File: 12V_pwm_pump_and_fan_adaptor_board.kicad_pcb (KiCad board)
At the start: 2 copper layers, 190 x 40 mm, 3 parts, among them J1 39-30-0080

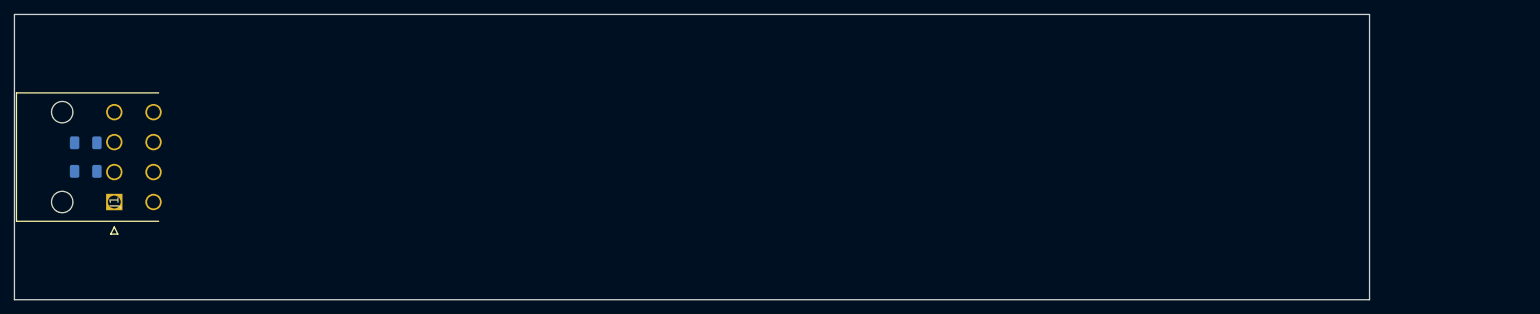
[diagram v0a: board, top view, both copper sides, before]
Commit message: feat: add connector footprint and update PCB layout and schematic files
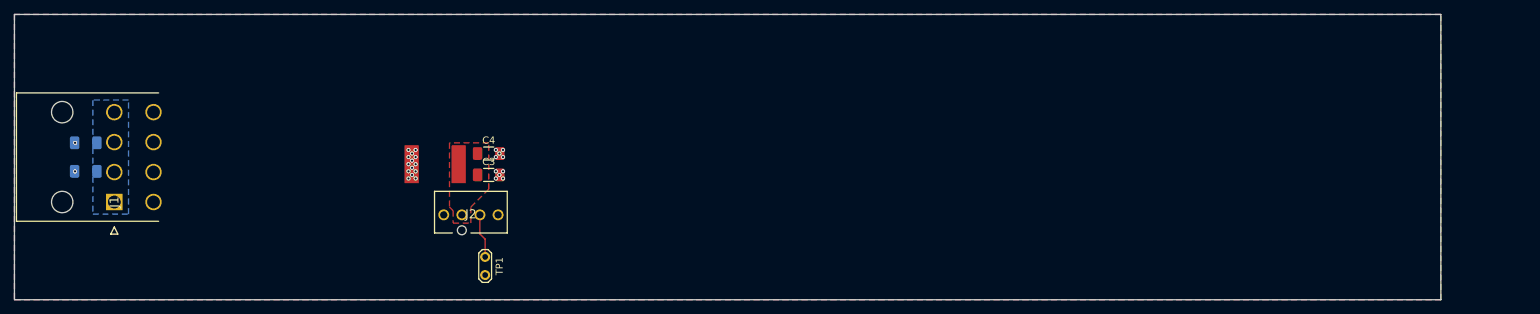
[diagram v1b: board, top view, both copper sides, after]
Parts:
- added C3: C, Capacitor_SMD:C_1206_3216Metric_Pad1.33x1.80mm_HandSolder, F.Cu at (86.5, 42.5)
- added C4: C, Capacitor_SMD:C_1206_3216Metric_Pad1.33x1.80mm_HandSolder, F.Cu at (86.5, 39.5)
- added FUSE1: ~, fuses:SMD2920P500TF16, F.Cu at (79.0, 41.0)
- added J2: Fan_4pin, connectors:0470531000, F.Cu at (80.2, 48.1)
- added TP1: TestPoint_2Pole, TestPoint:TestPoint_2Pads_Pitch2.54mm_Drill0.8mm, F.Cu at (86.0, 54.0)
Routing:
- net Net-(J2-TACH): track 0.00 -> 6.20 mm
- net GND: vias 0 -> 12
- net +12V: vias 0 -> 14
- added copper zone on B.Cu, net +12V
- added copper zone on In2.Cu, net +12V
- added copper zone on B.Cu, net GND
- added copper zone on F.Cu, net GND
- added copper zone on In1.Cu, net GND
- added copper zone on F.Cu, net Net-(J2-+12V)
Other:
- board size 190 x 40 mm -> 200 x 40 mm
- copper layers 2 -> 4

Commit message: feat: add 3D model for 350424-1 connector to library
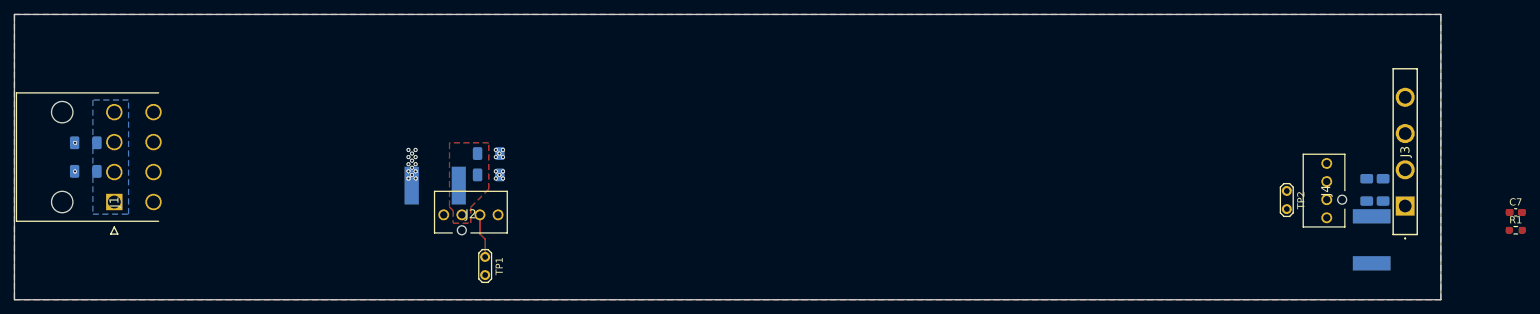
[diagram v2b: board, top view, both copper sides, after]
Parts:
- added C5: C, Capacitor_SMD:C_1206_3216Metric_Pad1.33x1.80mm_HandSolder, B.Cu at (209.6, 44.6)
- added C6: C, Capacitor_SMD:C_1206_3216Metric_Pad1.33x1.80mm_HandSolder, B.Cu at (211.9, 44.6)
- added C7: C, Capacitor_SMD:C_0603_1608Metric_Pad1.08x0.95mm_HandSolder, F.Cu at (230.5, 47.8)
- added FUSE2: ~, fuses:SMD2920P500TF16, B.Cu at (210.3, 51.6)
- added J3: 350424-1, connectors:350424-1, F.Cu at (215.0, 46.9)
- added J4: Fan_4pin, connectors:0470531000, F.Cu at (204.0, 48.5)
- added R1: R, Resistor_SMD:R_0603_1608Metric_Pad0.98x0.95mm_HandSolder, F.Cu at (230.5, 50.3)
- added TP2: TestPoint_2Pole, TestPoint:TestPoint_2Pads_Pitch2.54mm_Drill0.8mm, F.Cu at (198.4, 44.8)
- C3, C4, FUSE1: moved to B.Cu
- moved FUSE1 3.00 mm to (79.0, 44.0), turned to -90 degrees

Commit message: chore: update KiCad project settings and sync internal revision history
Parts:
- added C10: C, Capacitor_SMD:C_1206_3216Metric_Pad1.33x1.80mm_HandSolder, B.Cu at (116.1, 37.4)
- added C11: C, Capacitor_SMD:C_0603_1608Metric_Pad1.08x0.95mm_HandSolder, F.Cu at (115.9, 44.9)
- added C12: C, Capacitor_SMD:C_1206_3216Metric_Pad1.33x1.80mm_HandSolder, B.Cu at (138.9, 37.4)
- added C13: C, Capacitor_SMD:C_1206_3216Metric_Pad1.33x1.80mm_HandSolder, B.Cu at (146.1, 37.4)
- added C14: C, Capacitor_SMD:C_0603_1608Metric_Pad1.08x0.95mm_HandSolder, F.Cu at (145.9, 44.9)
- added C8: C, Capacitor_SMD:C_0603_1608Metric_Pad1.08x0.95mm_HandSolder, F.Cu at (85.9, 44.9)
- added C9: C, Capacitor_SMD:C_1206_3216Metric_Pad1.33x1.80mm_HandSolder, B.Cu at (108.9, 37.4)
- added FUSE3: ~, fuses:SMD2920P500TF16, B.Cu at (112.5, 31.8)
- added FUSE4: ~, fuses:SMD2920P500TF16, B.Cu at (142.5, 31.8)
- added J5: Fan_4pin, connectors:0470531000, F.Cu at (31.0, 55.2)
- added J6: Fan_4pin, connectors:0470531000, F.Cu at (110.0, 40.0)
- added J7: Fan_4pin, connectors:0470531000, F.Cu at (140.0, 40.0)
- added R2: R, Resistor_SMD:R_0603_1608Metric_Pad0.98x0.95mm_HandSolder, F.Cu at (86.7, 47.3)
- added R3: R, Resistor_SMD:R_0603_1608Metric_Pad0.98x0.95mm_HandSolder, F.Cu at (116.7, 47.3)
- added R4: R, Resistor_SMD:R_0603_1608Metric_Pad0.98x0.95mm_HandSolder, F.Cu at (146.7, 47.3)
- added TP3: TestPoint_2Pole, TestPoint:TestPoint_2Pads_Pitch2.54mm_Drill0.8mm, F.Cu at (112.4, 45.6)
- added TP4: TestPoint_2Pole, TestPoint:TestPoint_2Pads_Pitch2.54mm_Drill0.8mm, F.Cu at (142.4, 45.6)
- moved R1 33.9 mm to (196.7, 52.2)
- moved C7 31.5 mm to (199.2, 51.4), turned to 90 degrees
- moved FUSE1 12.7 mm to (82.5, 31.8), turned to 180 degrees
- moved TP1 9.16 mm to (82.4, 45.6), turned to 180 degrees
- moved J2 8.10 mm to (80.0, 40.0)
- moved C4 7.88 mm to (78.9, 37.4), turned to 180 degrees
- moved C3 5.12 mm to (86.1, 37.4)
- moved TP2 3.41 mm to (198.7, 48.1), turned to 90 degrees
- moved J4 2.82 mm to (204.1, 45.7), turned to -90 degrees
- moved C6 2.80 mm to (209.1, 44.7), turned to 90 degrees
- moved C5 2.10 mm to (211.7, 44.7), turned to 90 degrees
- moved FUSE2 0.22 mm to (210.4, 51.8), turned to 0 degrees
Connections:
- J2 pad 4: /output_connectors/12V_pwm_fan_output_connector/shared_pwm_signal -> Net-(J2-PWM)
- R1 pad 1: /output_connectors/12V_pwm_pump_connector/shared_pwm_signal -> /output_connectors/shared_pwm_signal
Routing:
- net /output_connectors/shared_pwm_signal: track 0.00 -> 161.7 mm
- net Net-(J4-PWM): track 0.00 -> 6.95 mm
- net Net-(J7-PWM): track 0.00 -> 6.77 mm
- net Net-(J6-PWM): track 0.00 -> 6.77 mm
- net Net-(J2-PWM): track 0.00 -> 6.77 mm
- net Net-(J7-TACH): track 0.00 -> 6.73 mm
- net Net-(J6-TACH): track 0.00 -> 6.73 mm
- net Net-(J4-TACH): track 0.00 -> 6.48 mm
- net Net-(J2-TACH): track 6.20 -> 6.73 mm
- net GND: vias 12 -> 43
- net +12V: vias 14 -> 0
- added copper zone on In2.Cu, net GND
- added copper zone on B.Cu, net Net-(J2-+12V)
- added copper zone on B.Cu, net Net-(J3-+12V)
- added copper zone on B.Cu, net Net-(J6-+12V)
- added copper zone on B.Cu, net Net-(J7-+12V)
- removed copper zone on In2.Cu, net +12V
- removed copper zone on F.Cu, net Net-(J2-+12V)

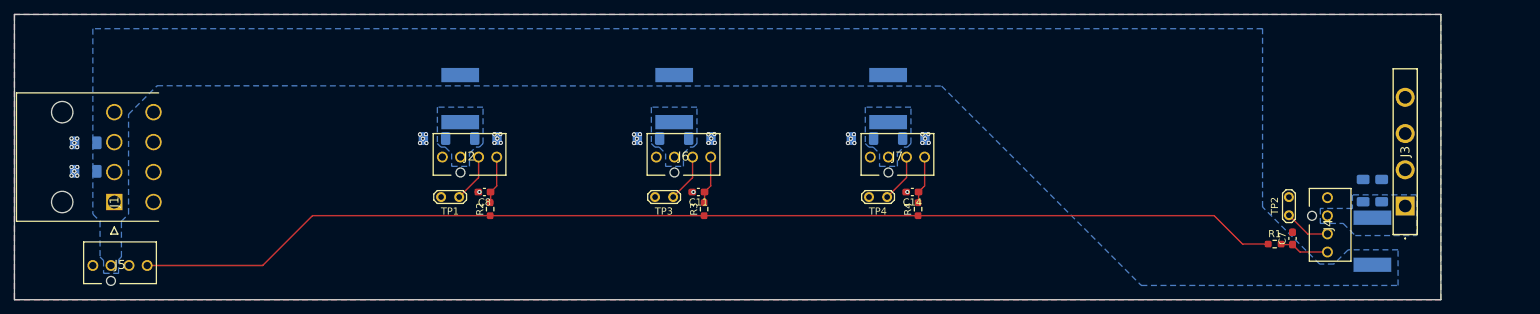
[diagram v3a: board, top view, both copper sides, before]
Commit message: feat: add Mol connectors and update schematic and PCB designs
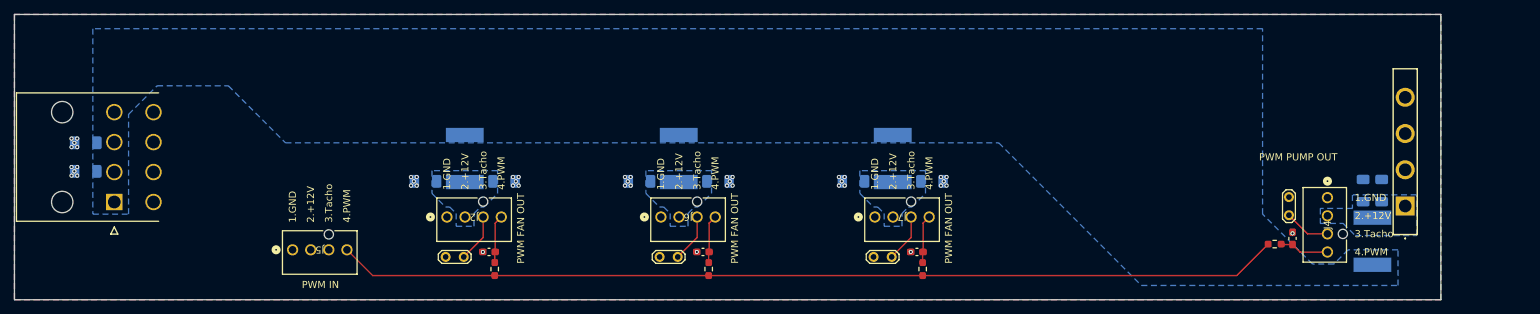
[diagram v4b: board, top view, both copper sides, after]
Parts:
- J2, J4, J5, J6, J7: footprint connectors:0470531000 -> connectors:CONN_SD-47053-001_H10p00_MOL
- moved J5 28.1 mm to (59.0, 53.0), turned to 180 degrees
- moved J7 8.43 mm to (140.6, 48.4), turned to 180 degrees
- moved R4 8.43 mm to (147.3, 55.7)
- moved TP4 8.43 mm to (143.0, 54.0)
- moved C11 8.43 mm to (116.5, 53.3)
- moved C14 8.43 mm to (146.5, 53.3)
- moved C8 8.43 mm to (86.5, 53.3)
- moved J2 8.43 mm to (80.6, 48.4), turned to 180 degrees
- moved J6 8.43 mm to (110.6, 48.4), turned to 180 degrees
- moved R2 8.43 mm to (87.3, 55.7)
- moved R3 8.43 mm to (117.3, 55.7)
- moved TP1 8.43 mm to (83.0, 54.0)
- moved TP3 8.43 mm to (113.0, 54.0)
- moved FUSE1 8.43 mm to (83.1, 40.2)
- moved FUSE3 8.43 mm to (113.1, 40.2)
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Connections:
- J5 pad 2: +12V -> unconnected-(J5-+12V-Pad2)
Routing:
- net /output_connectors/shared_pwm_signal: track 161.7 -> 132.5 mm
- net GND: vias 43 -> 44
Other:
- board text added: "PWM FAN OUT"
- board text added: "PWM IN"
- board text added: "PWM PUMP OUT"
